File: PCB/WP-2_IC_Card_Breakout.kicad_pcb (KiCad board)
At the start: 2 copper layers, 45 x 54 mm, 6 parts, among them J1 Conn_01x38_Female, J2 Conn_02x20_Odd_Even, U1 FLASH 256Kx8 5v Parallel, U2 FLASH 256Kx8 5v Parallel

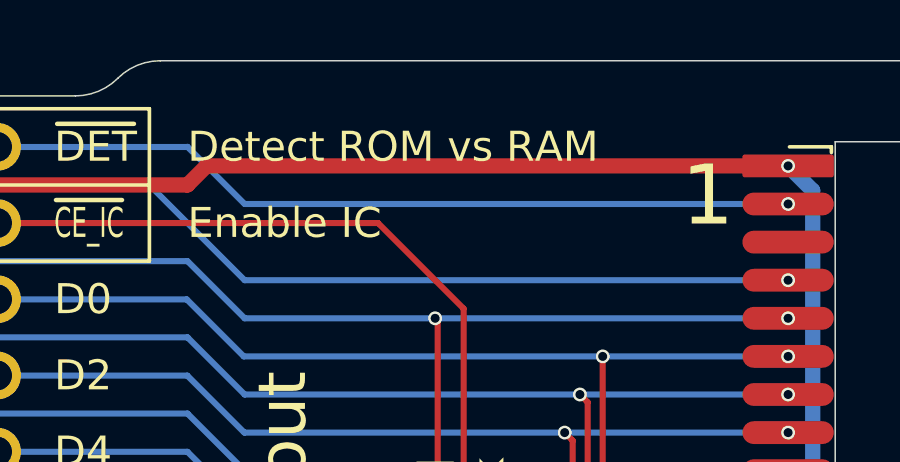
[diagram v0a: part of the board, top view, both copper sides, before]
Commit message: silkscreen on breakout card
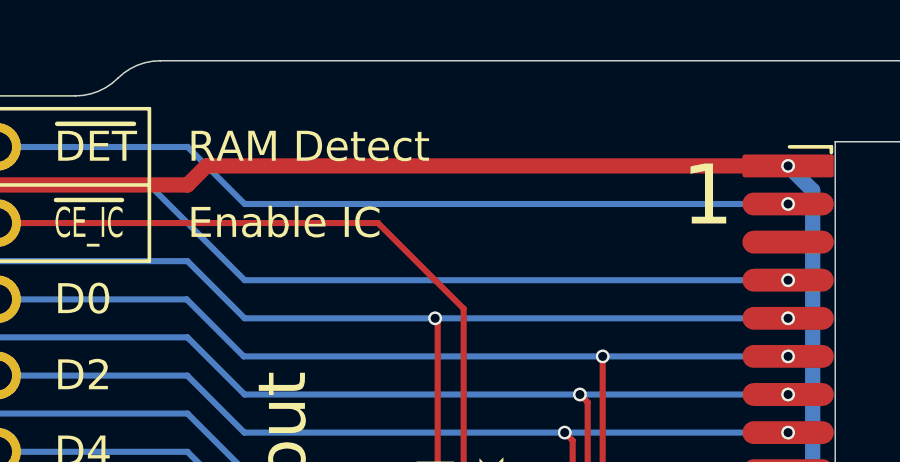
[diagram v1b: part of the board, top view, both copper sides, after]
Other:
- board text added: "RAM Detect"
- board text added: "WP-2_IC_Card_Breakout v003"
- board text removed: "Detect ROM vs RAM"
- board text removed: "WP-2_IC_Card_Breakout v002"

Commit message: kicad 6
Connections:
- net /R~W renamed /R~{W}
- net /~CE1 renamed /~{CE1}
- net /~CE_IC renamed /~{CE_IC}
- net /~DET renamed /~{DET}
- net /~OE renamed /~{OE}
- net /~WE_IC renamed /~{WE_IC}
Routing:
- net GND: track 79.6 -> 0.01 mm, vias 3 -> 6
- added copper zone on B.Cu, net GND
- added copper zone on F.Cu, net GND
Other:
- net class Default removed
- board text added: "PCB thickness 1.2mm"
- board text added: "R~{W}"
- board text added: "WP-2_IC_Card_Breakout v004"
- board text added: "~{CE1}"
- board text added: "~{CE_IC}"
- board text added: "~{DET}"
- board text added: "~{OE}"
- board text added: "~{WE_IC}"
- board text removed: "R~W"
- board text removed: "WP-2_IC_Card_Breakout v003"
- board text removed: "~CE1"
- board text removed: "~CE_IC"
- board text removed: "~DET"
- board text removed: "~OE"
- board text removed: "~WE_IC"
